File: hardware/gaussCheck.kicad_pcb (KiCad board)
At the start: 2 copper layers, 28 x 95.4 mm, 42 parts, among them J1 USB_C_Receptacle_USB2.0, J2 SWD, SW1 PTS810, SW2 CK KSC2, SW3 CK KSC2, SW4 CK KSC2, U1 TLV493D, U2 VIM-878-DP, U3 ATSAML22N18A-AUT, U4 TPS613221ADBV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

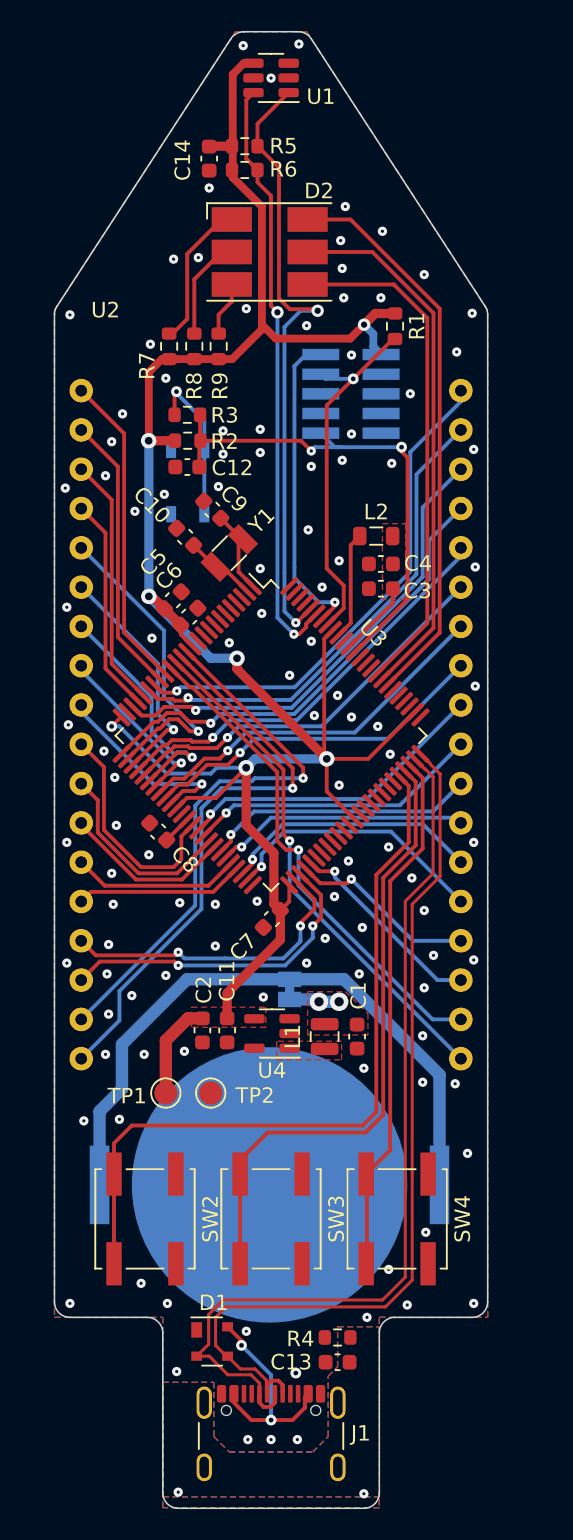
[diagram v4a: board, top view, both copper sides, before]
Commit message: moved buttons to the side JTAG to the bottom reset to the bottom
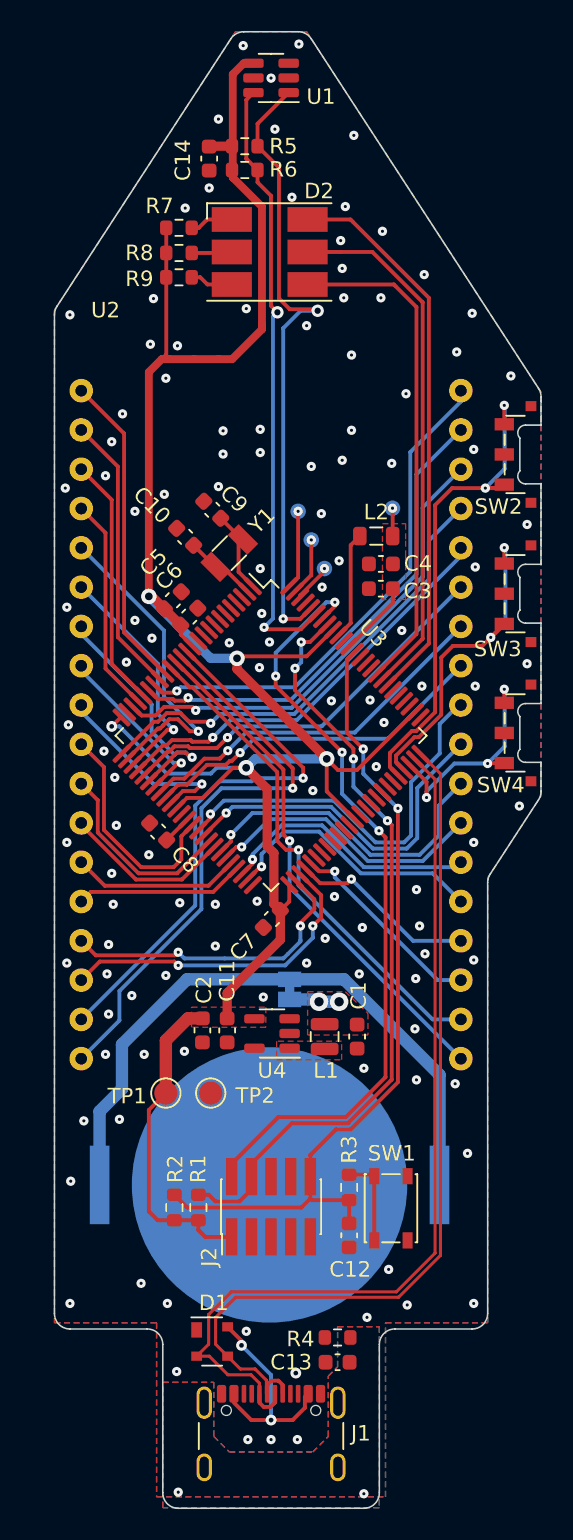
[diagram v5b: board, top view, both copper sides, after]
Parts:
- added TP3: TestPoint, TestPoint:TestPoint_Pad_D1.0mm, B.Cu at (107.8, 75.7)
- added TP4: TestPoint, TestPoint:TestPoint_Pad_D1.0mm, B.Cu at (103.5, 79.6)
- added TP5: TestPoint, TestPoint:TestPoint_Pad_D1.0mm, B.Cu at (101.8, 75.9)
- added TP6: TestPoint, TestPoint:TestPoint_Pad_D1.0mm, B.Cu at (102.6, 77.8)
- J2, SW1: moved to F.Cu
- SW2, SW3, SW4: value CK KSC2 -> PT847S; footprint Button_Switch_SMD:SW_Push_1P1T_NO_CK_KSC7xxJ -> GaussCheckCustomFootprint:SW_SPST_CK_PTS847MMxxxSMT_4.6x2.2mm
- moved R1 58.4 mm to (95.3, 120.9), turned to 90 degrees
- moved SW2 55.0 mm to (116.1, 72.2)
- moved J2 52.8 mm to (100.0, 120.8), turned to 90 degrees
- moved R3 51.0 mm to (105.0, 119.6), turned to 90 degrees
- moved C12 50.8 mm to (105.0, 122.7), turned to -90 degrees
- moved R2 49.6 mm to (93.8, 120.9), turned to 90 degrees
- moved SW1 48.7 mm to (107.8, 121.0)
- moved SW3 43.5 mm to (116.1, 81.2)
- moved SW4 32.4 mm to (116.1, 90.2)
- moved R7 7.69 mm to (94.0, 57.6), turned to 0 degrees
- moved R8 6.12 mm to (94.0, 59.2), turned to 0 degrees
- moved R9 5.15 mm to (94.0, 60.8), turned to 0 degrees
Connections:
- U3 pad 100: unconnected-(U3B-PB03-Pad100) -> Net-(U3B-PB03)
- U3 pad 98: unconnected-(U3B-PB1-Pad98) -> Net-(U3B-PB1)
- U3 pad 99: unconnected-(U3B-PB2-Pad99) -> Net-(U3B-PB2)
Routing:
- net /MCU/SWDIO: track 20.4 -> 50.1 mm, vias 1 -> 4
- net /MCU/SWCLK: track 23.6 -> 50.1 mm, vias 1 -> 4
- net /MCU/~{RESET}: track 33.3 -> 53.2 mm
- net /MCU/BTN3: track 34.2 -> 14.9 mm, vias 0 -> 3
- net /MCU/BTN2: track 40.6 -> 22.3 mm, vias 0 -> 2
- net /MCU/BTN1: track 48.5 -> 32.2 mm, vias 0 -> 2
- net +3V3: track 147.3 -> 155.3 mm, vias 7 -> 5
- net Net-(D2-RK): track 9.57 -> 2.81 mm
- net /MCU/MNGH5: track 20.5 -> 25.9 mm
- net Net-(U3B-PB03): track 0.00 -> 5.08 mm, vias 0 -> 1
- net Net-(R3-Pad2): track 10.3 -> 5.82 mm, vias 1 -> 0
- net /MCU/DPCBA5: track 19.1 -> 23.2 mm
- net Net-(D2-GK): track 6.66 -> 2.61 mm
- net Net-(U3B-PB2): track 0.00 -> 3.79 mm, vias 0 -> 1
- net /MCU/MNGH6: track 17.7 -> 21.0 mm
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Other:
- board size 28 x 95.4 mm -> 31.5 x 95.4 mm

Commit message: added 3V3 LDO added VBat Measurement
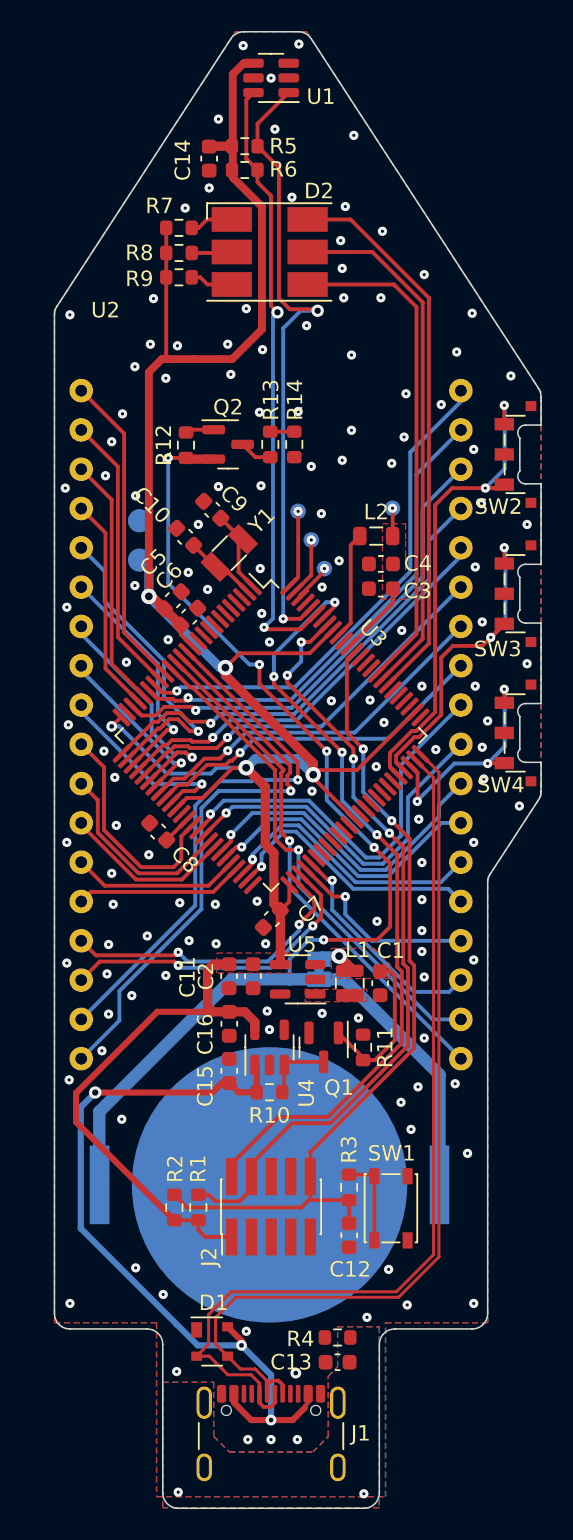
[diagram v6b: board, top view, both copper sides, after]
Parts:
- added C15: 1u, Capacitor_SMD:C_0603_1608Metric, F.Cu at (97.3, 112.1)
- added C16: 1u, Capacitor_SMD:C_0603_1608Metric, F.Cu at (97.3, 109.0)
- added Q1: BSS138, Package_TO_SOT_SMD:SOT-23, F.Cu at (103.4, 110.5)
- added Q2: BSS83P, Package_TO_SOT_SMD:SOT-23, F.Cu at (97.2, 71.6)
- added R10: 10k, Resistor_SMD:R_0603_1608Metric, F.Cu at (99.9, 113.5)
- added R11: 100k, Resistor_SMD:R_0603_1608Metric, F.Cu at (106.0, 110.5)
- added R12: 100k, Resistor_SMD:R_0603_1608Metric, F.Cu at (94.5, 71.6)
- added R13: 4k7, Resistor_SMD:R_0603_1608Metric, F.Cu at (100.0, 71.6)
- added R14: 10k, Resistor_SMD:R_0603_1608Metric, F.Cu at (101.5, 71.6)
- added U5: TPS613221ADBV, Package_TO_SOT_SMD:SOT-23-5, F.Cu at (101.7, 106.2)
- TP1, TP2: moved to B.Cu
- U4: value TPS613221ADBV -> AP2112K-3.3
- moved TP2 37.3 mm to (91.5, 76.5), turned to 180 degrees
- moved TP1 34.5 mm to (91.5, 79.0), turned to 180 degrees
- moved C2 4.79 mm to (98.8, 106.0)
- moved L1 3.81 mm to (105.1, 106.4)
- moved C1 3.76 mm to (107.0, 106.4)
- moved C11 3.50 mm to (97.3, 106.0)
- moved JP1 2.30 mm to (103.1, 105.5), turned to 90 degrees
- moved U4 0.91 mm to (99.9, 110.5), turned to 90 degrees
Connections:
- net /BATT renamed /Power/BATT
- L1 pad 2: /BATT_SW -> /Power/BATT_SW
- U3 pad 5: unconnected-(U3C-PC02/I10/AIN18-Pad5) -> /MCU/Sense_VBat
- U4 pad 1: /BATT_SW -> VBUS
- U4 pad 3: unconnected-(U4-NC-Pad3) -> Net-(Q1-D)
- U4 pad 4: +3V3 -> unconnected-(U4-NC-Pad4)
- U4 pad 5: unconnected-(U4-NC-Pad5) -> +3V3
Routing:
- net +BATT: track 41.6 -> 88.2 mm, vias 0 -> 5
- net VBUS: track 13.5 -> 49.0 mm, vias 2 -> 3
- net +3V3: track 155.3 -> 166.8 mm
- net /Power/BATT: track 3.26 -> 12.9 mm, vias 2 -> 1
- net Net-(Q1-D): track 0.00 -> 4.45 mm
- net Net-(Q2-D): track 0.00 -> 2.13 mm
- net /Power/EN_VBat: track 0.00 -> 1.86 mm
- net /Power/Sense_VBat: track 0.00 -> 1.55 mm
- net /MCU/DPCBA8: track 13.0 -> 14.6 mm
- net /MCU/DPCBA6: track 18.4 -> 19.2 mm
- net /MCU/MNGH7: track 17.1 -> 17.9 mm
- net /MCU/SWCLK: track 50.1 -> 50.7 mm
- net /MCU/BTN3: track 14.9 -> 15.4 mm
- net GND: vias 122 -> 135
- added copper zone on F.Cu, net /Power/BATT_SW
- removed copper zone on F.Cu, net /BATT_SW

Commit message: added schottky diode to LDO connected en_vbat signal added a drawing of mems axis
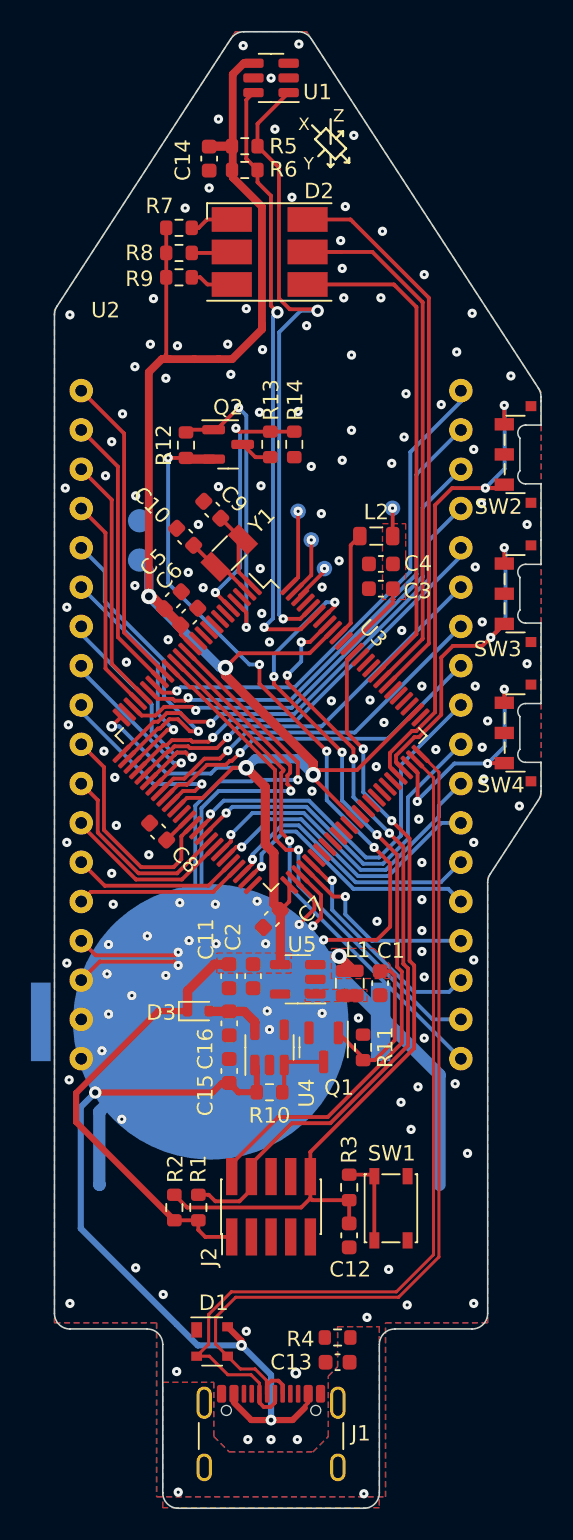
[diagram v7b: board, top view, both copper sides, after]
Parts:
- added D3: RB521S30T1G, Diode_SMD:D_SOD-523, F.Cu at (95.3, 108.2)
- moved BT1 11.2 mm to (96.1, 108.9)
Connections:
- C16 pad 1: +3V3 -> Net-(D3-A)
- Q2 pad 1: /Power/EN_VBat -> /MCU/EN_VBat
- R12 pad 2: /Power/EN_VBat -> /MCU/EN_VBat
- R13 pad 2: /Power/Sense_VBat -> /MCU/Sense_VBat
- R14 pad 2: /Power/Sense_VBat -> /MCU/Sense_VBat
- U3 pad 4: unconnected-(U3C-PC01/I9/AIN17-Pad4) -> /MCU/EN_VBat
- U4 pad 5: +3V3 -> Net-(D3-A)
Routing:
- net /MCU/EN_VBat: track 0.00 -> 20.3 mm, vias 0 -> 2
- net /MCU/Sense_VBat: track 0.00 -> 16.7 mm, vias 0 -> 2
- net +3V3: track 166.8 -> 162.0 mm
- net Net-(D3-A): track 0.00 -> 3.72 mm
- net /Power/EN_VBat: track 1.86 -> 0.00 mm
- net /Power/Sense_VBat: track 1.55 -> 0.00 mm
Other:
- board text added: "X"
- board text added: "Y"
- board text added: "Z"

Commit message: fixed Batposition DRC checked!
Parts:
- moved BT1 11.2 mm to (99.9, 119.5)
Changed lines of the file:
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@@
   )
   (footprint "Battery:BatteryHolder_Keystone_3034_1x20mm" (layer "B.Cu")
-    (at 96.1 108.9 180)
+    (at 99.9 119.45 180)
     (descr "Keystone 3034 SMD battery holder for 2020, 2025 and 2032 coincell batteries. http://www.keyelco.com/product-pdf.cfm?p=798")
     (tags "Keystone type 3034 coin cell retainer")
